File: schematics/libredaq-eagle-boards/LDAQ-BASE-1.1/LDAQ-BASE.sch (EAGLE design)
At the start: 107 parts, among them Q1 FDV301N, Q2 FDV301N, Q3 FDV301N, Q4 FDV301N, Q5 FDV301N, Q6 FDV301N, Q7 FDV301N, T1 FDN340P, U1 ATSAM3U1CB, U2 LM3671MF-3.3, U4 ISL3175, U6 MCP16322, U8 LMV321, X1 PJ-102A, Y1 12M

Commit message: update from local copy
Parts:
- removed D1: D1, diode:DIODE-SMB
- removed U6: MCP16322, libredaq-comps:MCP16322
- removed X1: PJ-102A, SmartPrj:POWERSUPPLY_DC21MMX
- added D2: FM4004W-W, FM4004W-W:FM4004W-W
- added J1: PJ-102A, PJ-102A:PJ-102A
- added U3: TS30012-M050QFNR, TS30012-M050QFNR:TS30012-M050QFNR
- JP6: value SCREWTERMINAL-3.5MM-3 -> 691214110003; device libredaq-comps:SCREWTERMINAL-3.5MM-3 -> 691214110003:691214110003
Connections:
- removed net N$16: C10.2, L5.1, U6.SW@1, U6.SW@12, U6.SW@13, U6.SW@16
- new net FB_PWR5: C10.2, L5.1, U3.VSW_1, U3.VSW_2, U3.VSW_3, U3.VSW_4
- net +5V: now also U3.FB; no longer U6.VFB
- net GND: now also J1.2, J1.3, U3.EP, U3.PGND_1, U3.PGND_2; no longer U6.EXPAD, U6.PGND@14, U6.PGND@15, U6.SGND, X1.1, X1.3
- net N$17: now also U3.BST; no longer U6.BOOST
- net PWRIN: now also D2.A, J1.1; no longer D1.A, X1.2
- net VIN: now also D2.K, U3.VCC_1, U3.VCC_2, U3.VCC_3; no longer D1.C, U6.VIN@11, U6.VIN@2, U6.VIN@3
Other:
- moved on the sheet: C21, C22, JP6, PC1

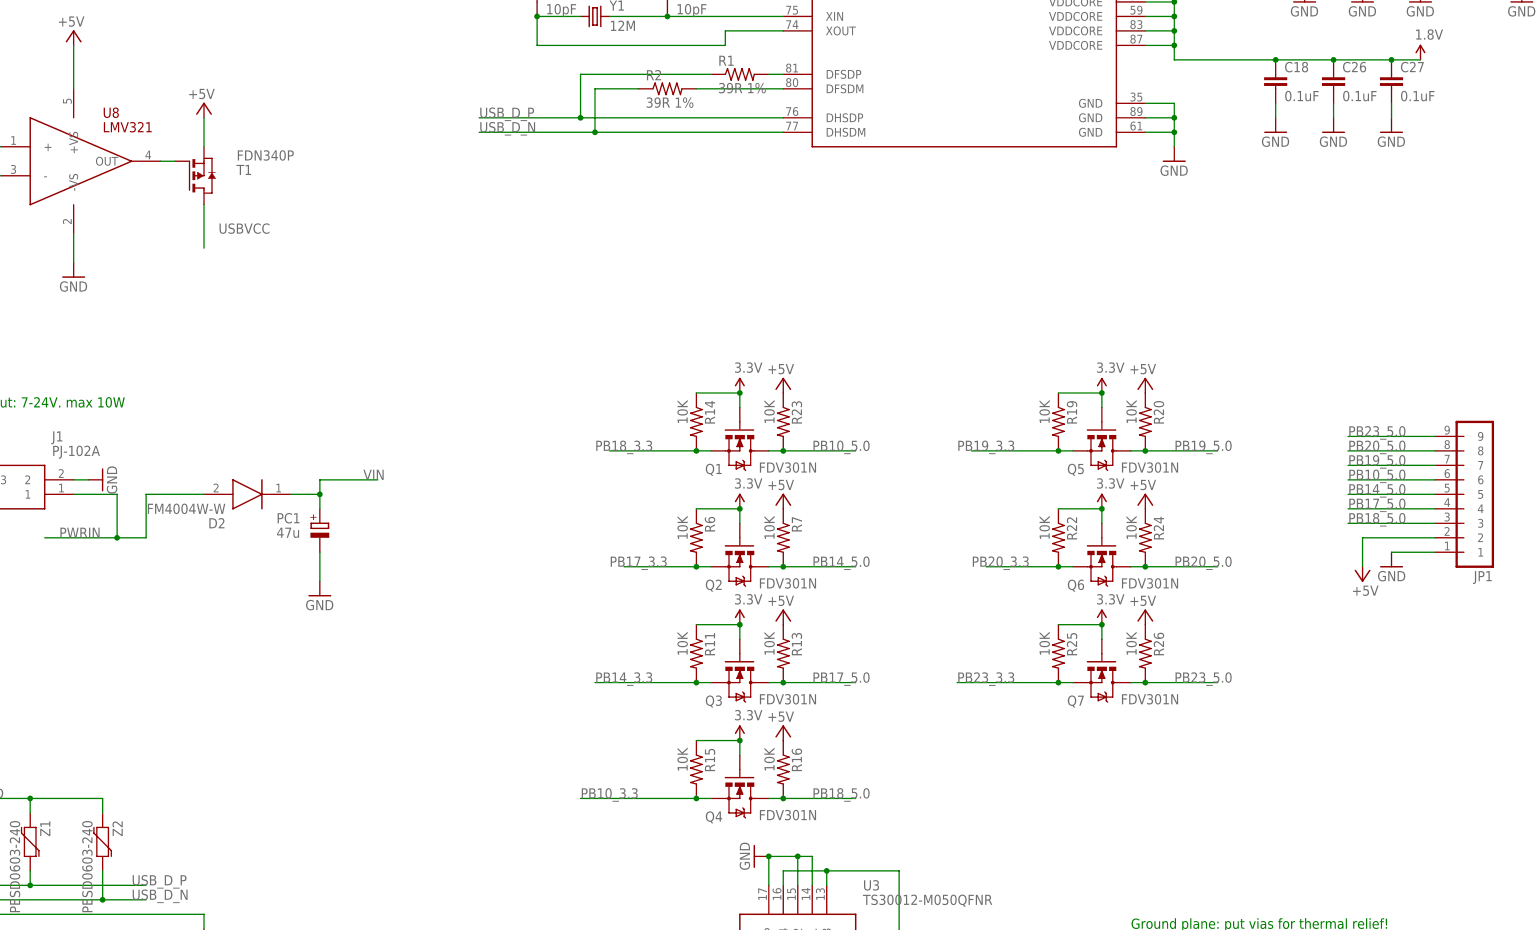
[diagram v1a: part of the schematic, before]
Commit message: base board: use bidirectional 3.3-5V driver
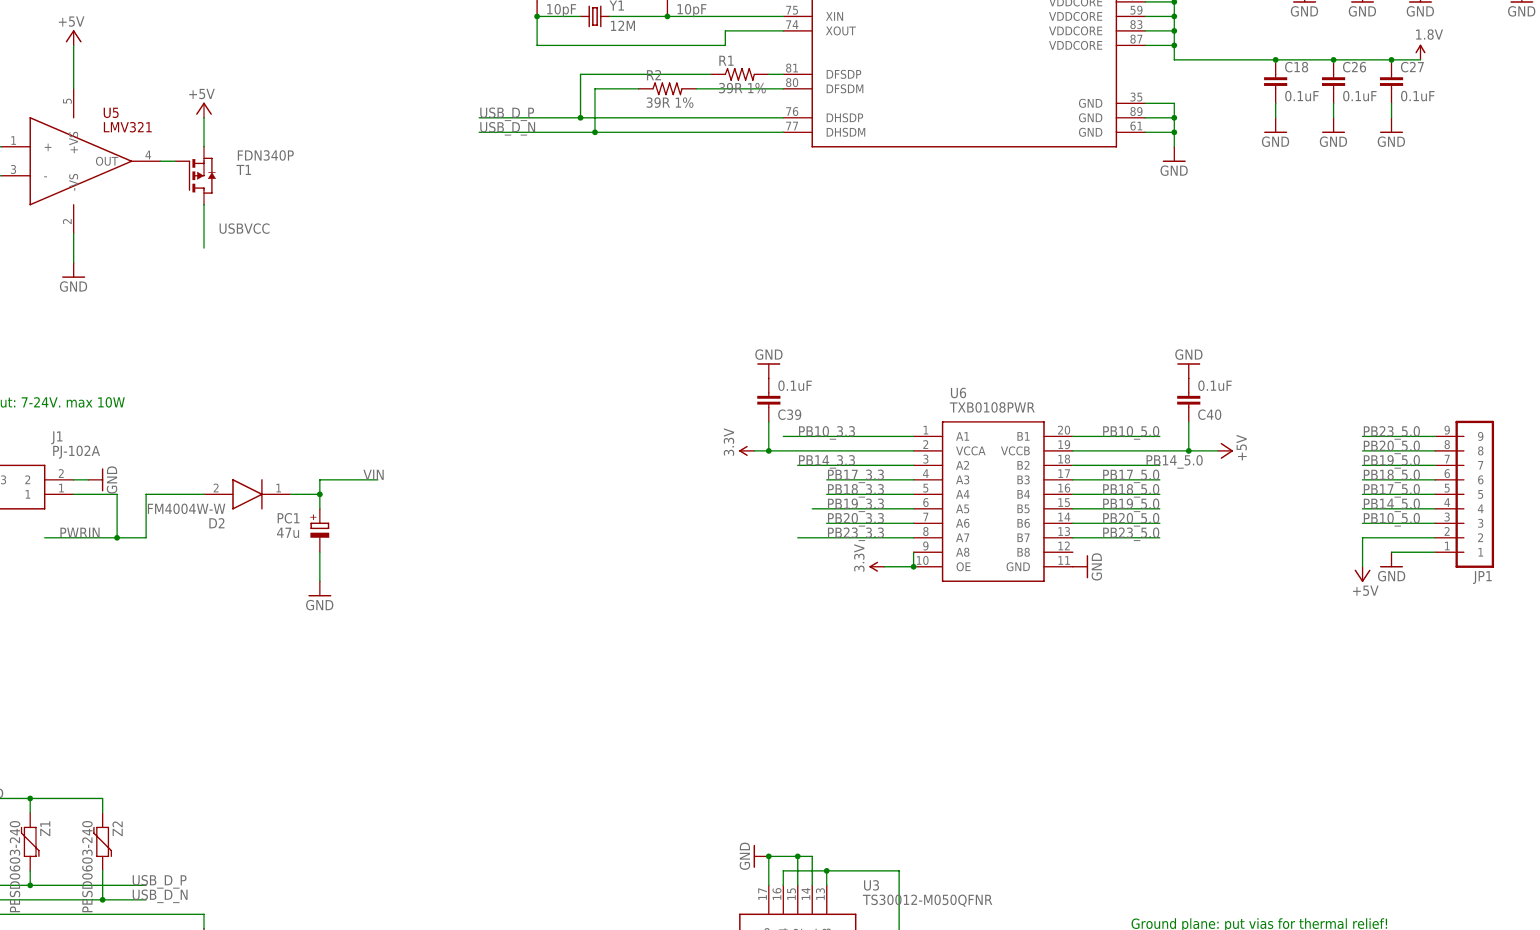
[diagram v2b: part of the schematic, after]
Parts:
- removed Q1, Q2, Q3, Q4, Q5, Q6, Q7: FDV301N, SparkFun:MOSFET-NCHANNELSMD
- removed R11, R13, R14, R15, R16, R19, R20, R22, R23, R24, R25, R26, R6, R7: 10K, SparkFun:RESISTOR0603-RES
- added C39, C40: 0.1uF, SparkFun-Capacitors:0.1UF-25V(+80/-20%)(0603)
- added U6: TXB0108PWR, TXB0108PWR:TXB0108PWR
- renumbered U8 to U5
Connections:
- net +5V: now also C40.1, U6.VCCB; no longer R13.1, R16.1, R20.1, R23.1, R24.1, R26.1, R7.1
- net 3.3V: now also C39.1, U6.A8, U6.OE, U6.VCCA; no longer Q1.G, Q2.G, Q3.G, Q4.G, Q5.G, Q6.G, Q7.G, R11.1, R14.1, R15.1, R19.1, R22.1, R25.1, R6.1
- net GND: now also C39.2, C40.2, U6.GND
- net PB10_3.3: now also U6.A1; no longer Q4.S, R15.2
- net PB10_5.0: now also JP1.3, U6.B1; no longer JP1.6, Q1.D, R23.2
- net PB14_3.3: now also U6.A2; no longer Q3.S, R11.2
- net PB14_5.0: now also JP1.4, U6.B2; no longer JP1.5, Q2.D, R7.2
- net PB17_3.3: now also U6.A3; no longer Q2.S, R6.2
- net PB17_5.0: now also JP1.5, U6.B3; no longer JP1.4, Q3.D, R13.2
- net PB18_3.3: now also U6.A4; no longer Q1.S, R14.2
- net PB18_5.0: now also JP1.6, U6.B4; no longer JP1.3, Q4.D, R16.2
- net PB19_3.3: now also U6.A5; no longer Q5.S, R19.2
- net PB19_5.0: now also U6.B5; no longer Q5.D, R20.2
- net PB20_3.3: now also U6.A6; no longer Q6.S, R22.2
- net PB20_5.0: now also U6.B6; no longer Q6.D, R24.2
- net PB23_3.3: now also U6.A7; no longer Q7.S, R25.2
- net PB23_5.0: now also U6.B7; no longer Q7.D, R26.2

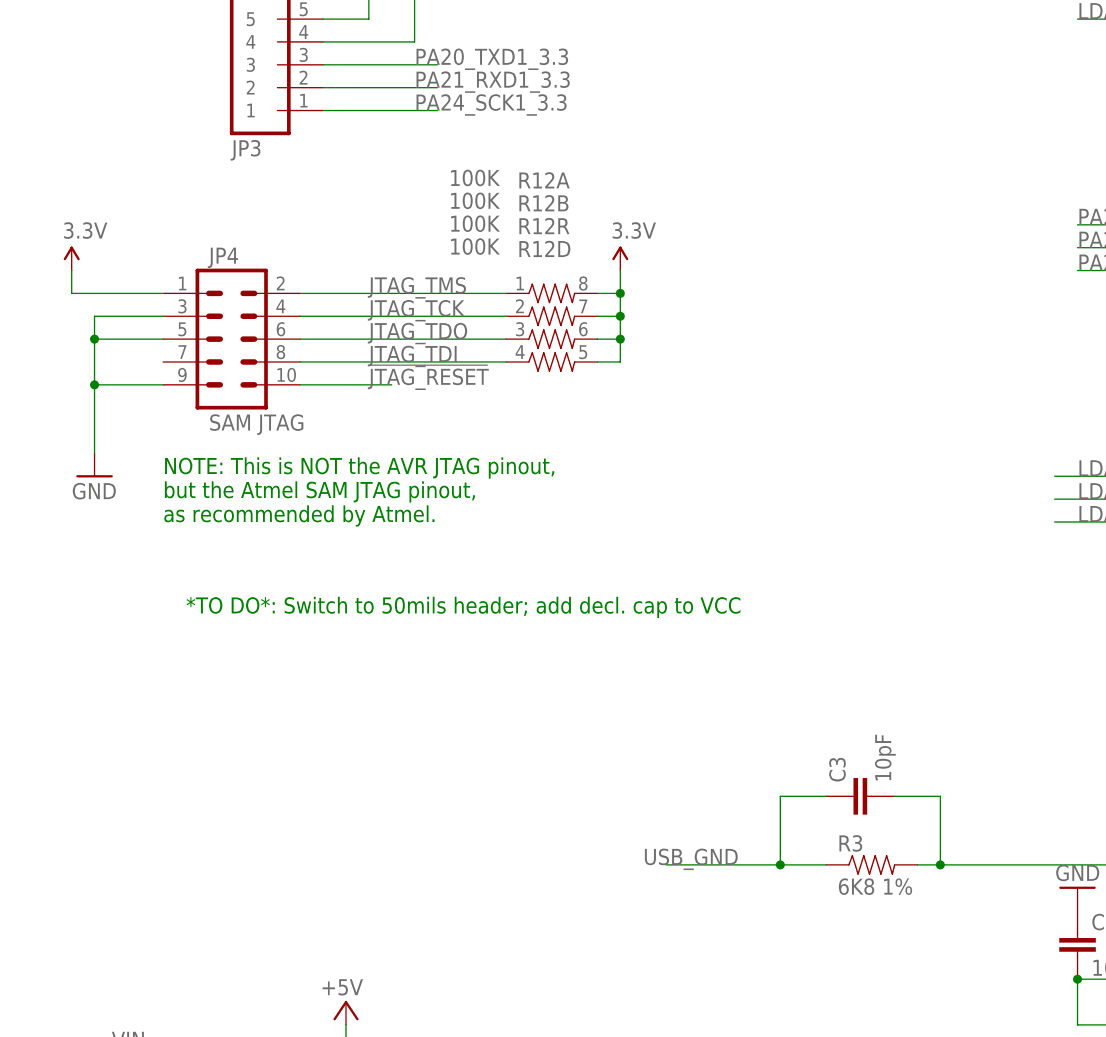
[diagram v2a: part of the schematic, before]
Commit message: Base: Use JTAG 50mils connector
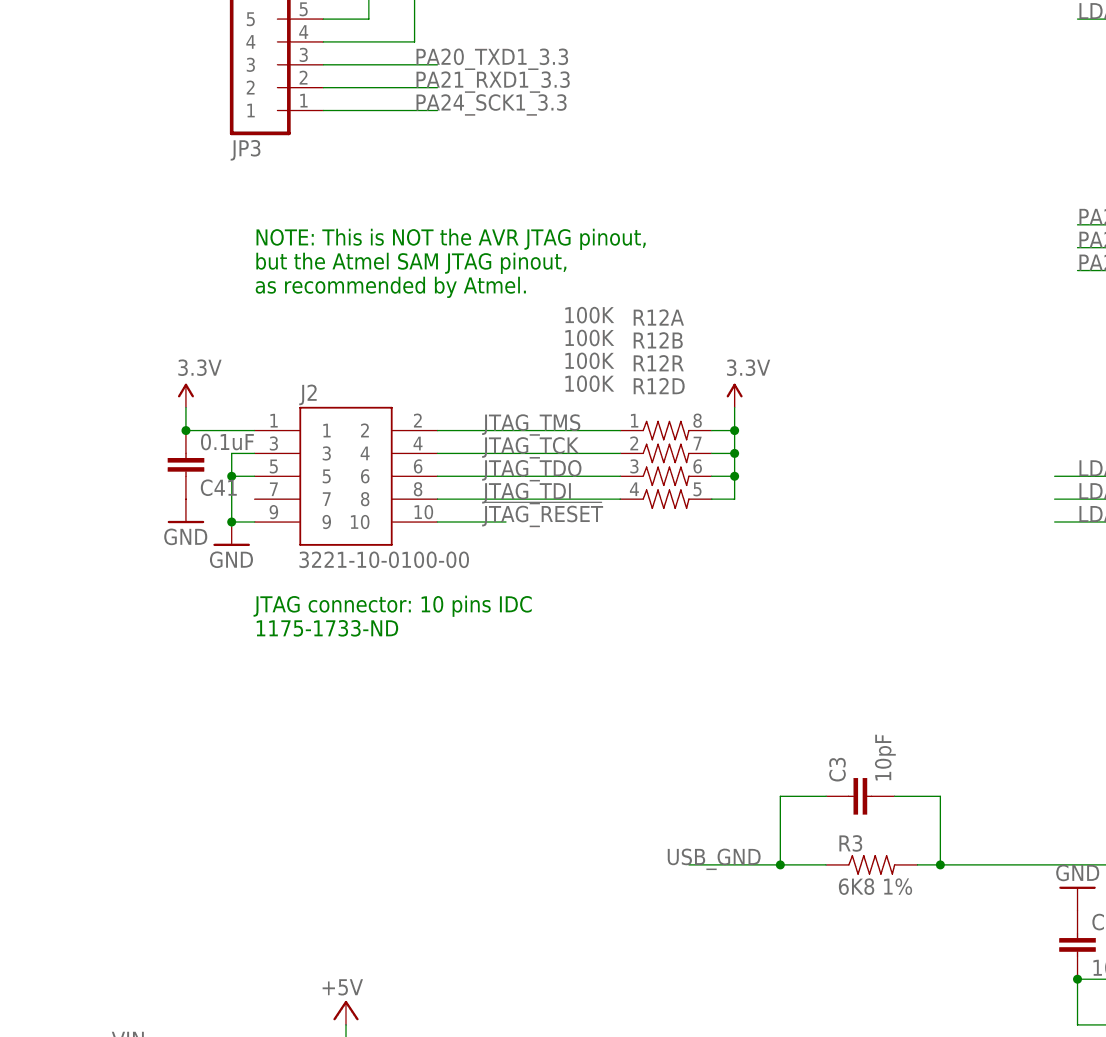
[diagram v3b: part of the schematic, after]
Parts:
- removed JP4: SAM JTAG, SparkFun-Connectors:M05X2PTH
- added C41: 0.1uF, SparkFun-Capacitors:0.1UF-25V(+80/-20%)(0603)
- added J2: 3221-10-0100-00, 3221-10-0100-00:3221-10-0100-00
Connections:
- net !JTAG_RESET: now also J2.10; no longer JP4.10
- net 3.3V: now also C41.2, J2.1; no longer JP4.1
- net GND: now also C41.1, J2.3, J2.5, J2.9; no longer JP4.3, JP4.5, JP4.9
- net JTAG_TCK: now also J2.4; no longer JP4.4
- net JTAG_TDI: now also J2.8; no longer JP4.8
- net JTAG_TDO: now also J2.6; no longer JP4.6
- net JTAG_TMS: now also J2.2; no longer JP4.2
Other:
- note added: "JTAG connector: 10 pins IDC 1175-1733-ND"
- note removed: "*TO DO*: Switch to 50mils header; add decl. cap to VCC"
- moved on the sheet: R12A, R12B, R12D, R12R
